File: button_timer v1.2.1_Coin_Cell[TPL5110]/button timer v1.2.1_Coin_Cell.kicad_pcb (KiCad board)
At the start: 2 copper layers, 21 x 47.8 mm, 24 parts, among them J1 Conn_01x05_Female, SW1 SW_Push, SW2 SW_Push, U1 TPS61097A, U3 TPL5111, X1 ESP-12E

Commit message: :rocket: :full_moon_with_face:
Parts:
- removed U3: TPL5111, handsolder:SOT-23-6handsoldering
- added Q1: TSM2323, Package_TO_SOT_SMD:SOT-23, F.Cu at (126.2, 64.5)
- added U2: TPL5110, handsolder:SOT-23-6handsoldering, B.Cu at (125.7, 59.0)
- C4, R8: moved to B.Cu
- C5: moved to F.Cu
- moved C4 12.6 mm to (125.4, 55.7)
- moved R7 8.05 mm to (129.6, 65.0), turned to 90 degrees
- moved SW1 7.66 mm to (128.8, 60.5), turned to 180 degrees
- moved C5 6.44 mm to (125.7, 62.0), turned to 0 degrees
- moved R8 5.66 mm to (121.7, 58.7)
- moved C3 1.86 mm to (134.8, 68.2), turned to 270 degrees
- moved L1 0.22 mm to (133.3, 60.9)
- turned D2 to 0 degrees
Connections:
- L1 pad 1: Net-(BT1-Pad1) -> Net-(L1-Pad1)
- R7 pad 2: Net-(R7-Pad2) -> Net-(L1-Pad1)
- U1 pad 1: Net-(BT1-Pad1) -> Net-(L1-Pad1)
- U1 pad 3: Net-(R7-Pad2) -> Net-(R7-Pad1)
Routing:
- net /GPIO4: track 12.2 -> 38.8 mm, vias 2 -> 1
- net Net-(BT1-Pad1): track 39.6 -> 13.5 mm, vias 9 -> 2
- net /GND: track 99.7 -> 82.7 mm, vias 18 -> 11
- net /VCC: track 55.9 -> 39.7 mm
- net Net-(Q1-Pad1): track 0.00 -> 12.3 mm, vias 0 -> 1
- net Net-(R7-Pad2): track 10.9 -> 0.00 mm, vias 1 -> 0
- net Net-(L1-Pad1): track 0.00 -> 8.00 mm, vias 0 -> 1
- net /RST: track 54.7 -> 48.7 mm, vias 4 -> 2
- net /GPIO0: track 9.39 -> 14.7 mm, vias 3 -> 0
- net Net-(R7-Pad1): track 0.00 -> 4.16 mm
- net /EN: track 18.0 -> 15.3 mm, vias 3 -> 0
- net Net-(R6-Pad2): track 16.0 -> 14.5 mm, vias 1 -> 0
- net /RX: track 7.95 -> 9.34 mm
- net Net-(D2-Pad2): track 3.24 -> 4.04 mm
- net /TX: track 14.6 -> 14.2 mm, vias 5 -> 0
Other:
- board text added: "Button - Coin Cell v.1.2.1 TPL5110"
- board text added: "V.1.2.1 ONLY COIN CELL TIMER TPL5110"
- board text removed: "Button - Coin Cell v.1.2.1"
- board text removed: "V.1.2.1 ONLY COIN CELL TIMER TPL5111"

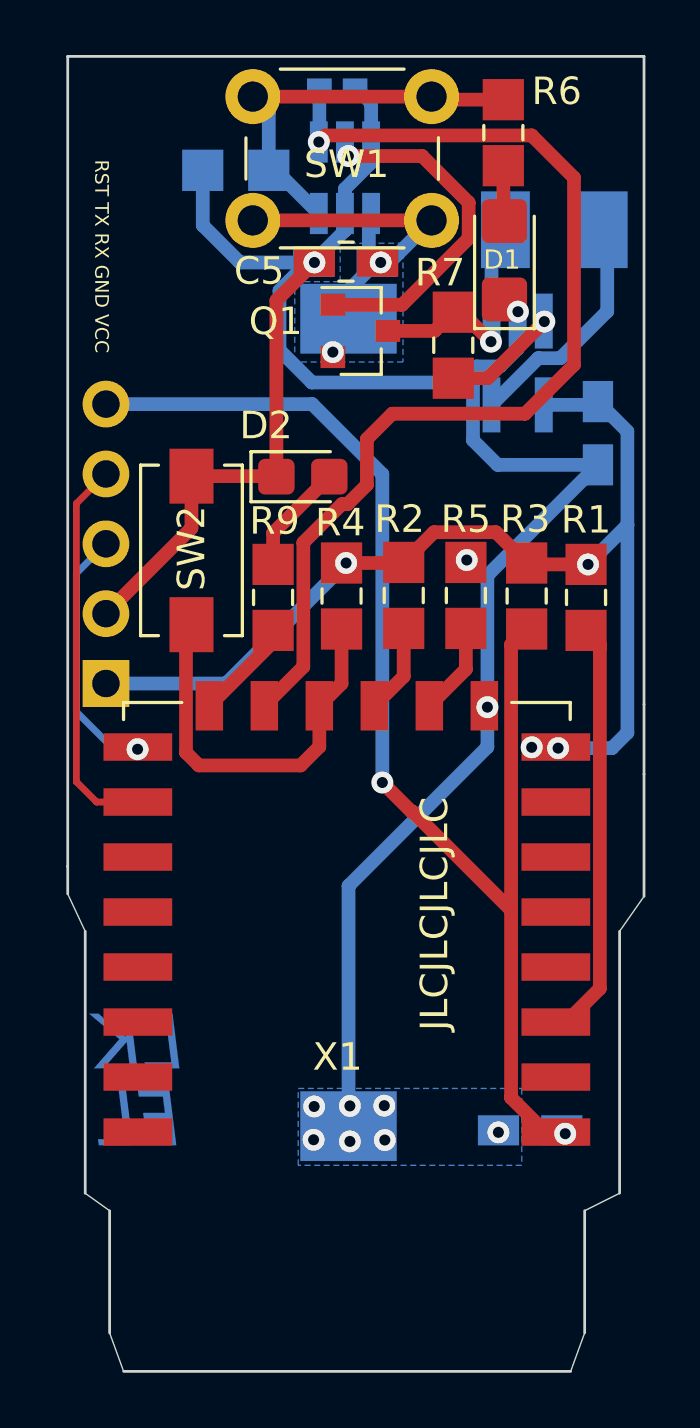
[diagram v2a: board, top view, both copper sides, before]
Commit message: 3D Models etwas verbessert
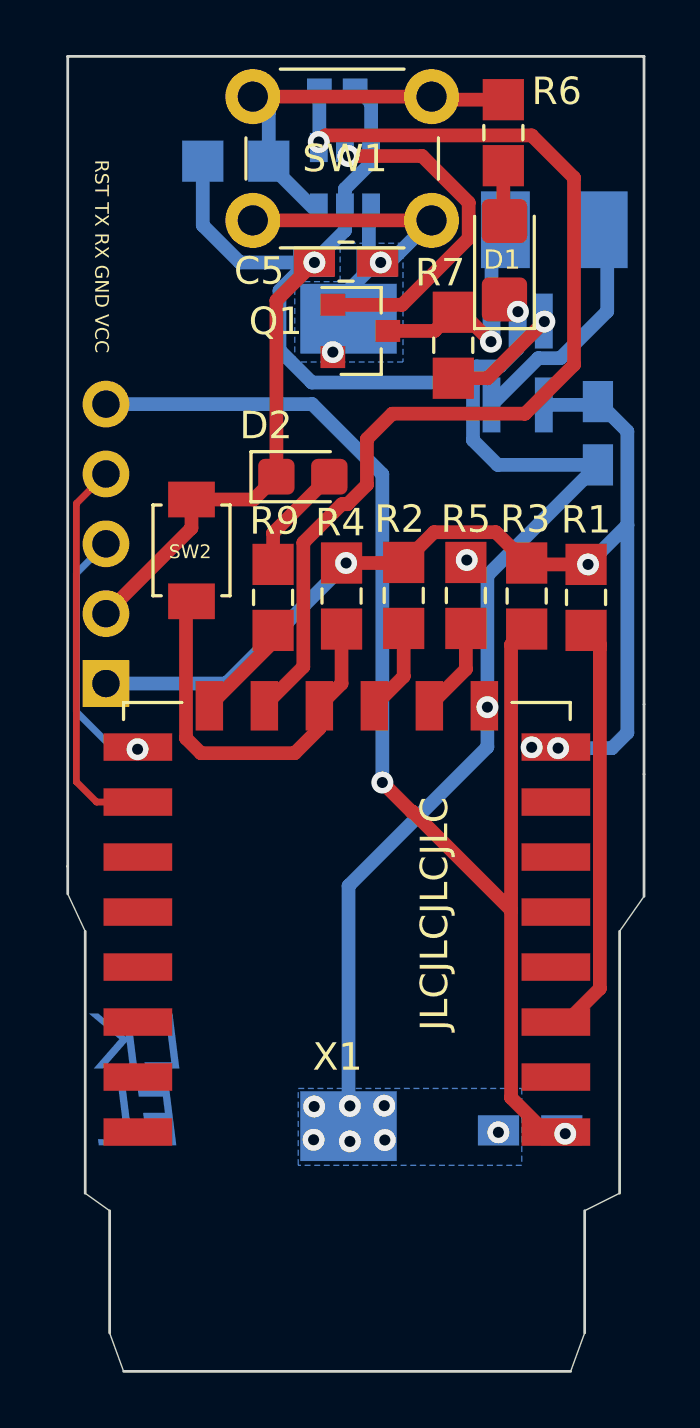
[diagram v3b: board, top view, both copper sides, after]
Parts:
- J1: footprint Connector_PinHeader_2.54mm:PinHeader_1x05_P2.54mm_Vertical -> handsolder:PinSocket_1x05_P2.54mm_Vertical_mod
- SW1: footprint Button_Switch_THT:SW_PUSH_6mm -> handsolder:SW_PUSH_6mm_H8mm_mod
- SW2: footprint Button_Switch_SMD:SW_SPST_EVQPE1 -> handsolder:SW_SPST_B3U-1000P_mod
- U2: footprint handsolder:SOT-23-6handsoldering -> Package_TO_SOT_SMD:SOT-23-6
- moved R8 0.33 mm to (121.7, 58.4)

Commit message: Silkscreen Update
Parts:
- D2: footprint LED_SMD:LED_0805_2012Metric_Castellated -> handsolder:LED_0805_2012Metric_Castellated_mod
- U2: footprint Package_TO_SOT_SMD:SOT-23-6 -> handsolder:SOT-23-6handsoldering

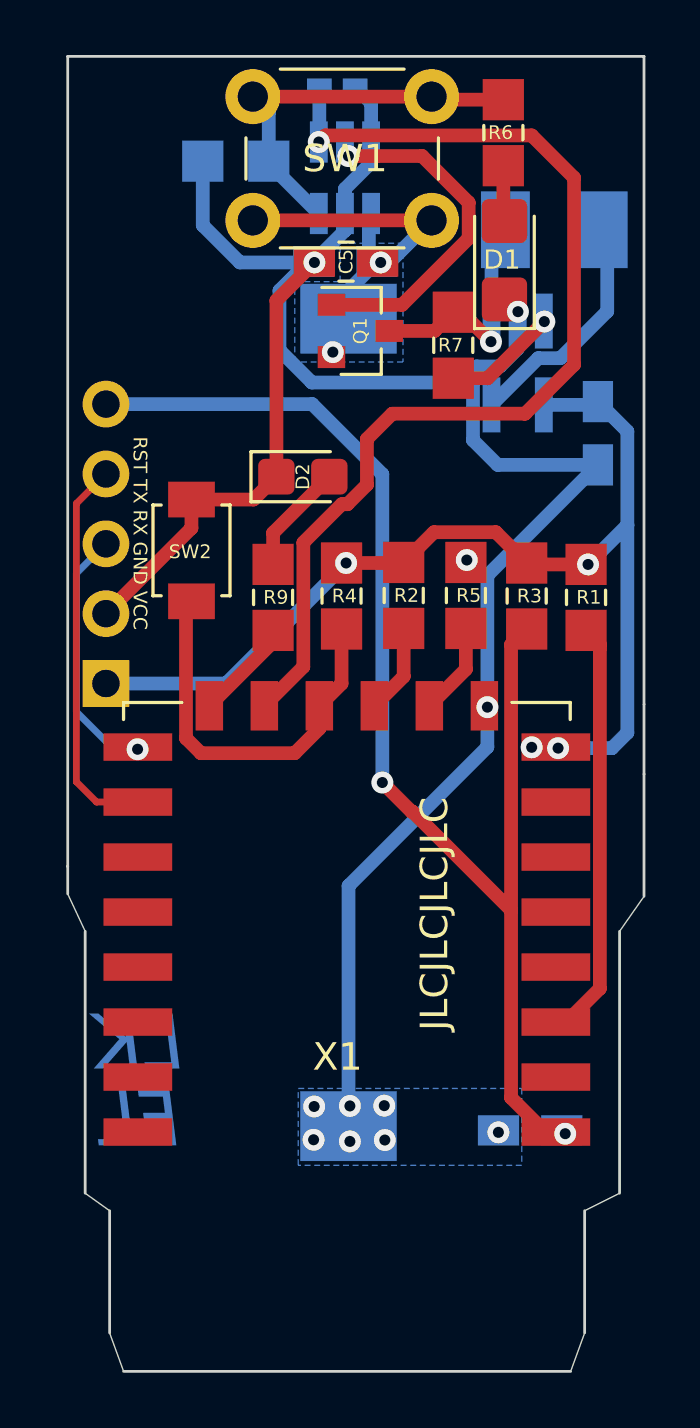
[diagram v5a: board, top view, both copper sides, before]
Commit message: cap added between vcc and gnd of the esp
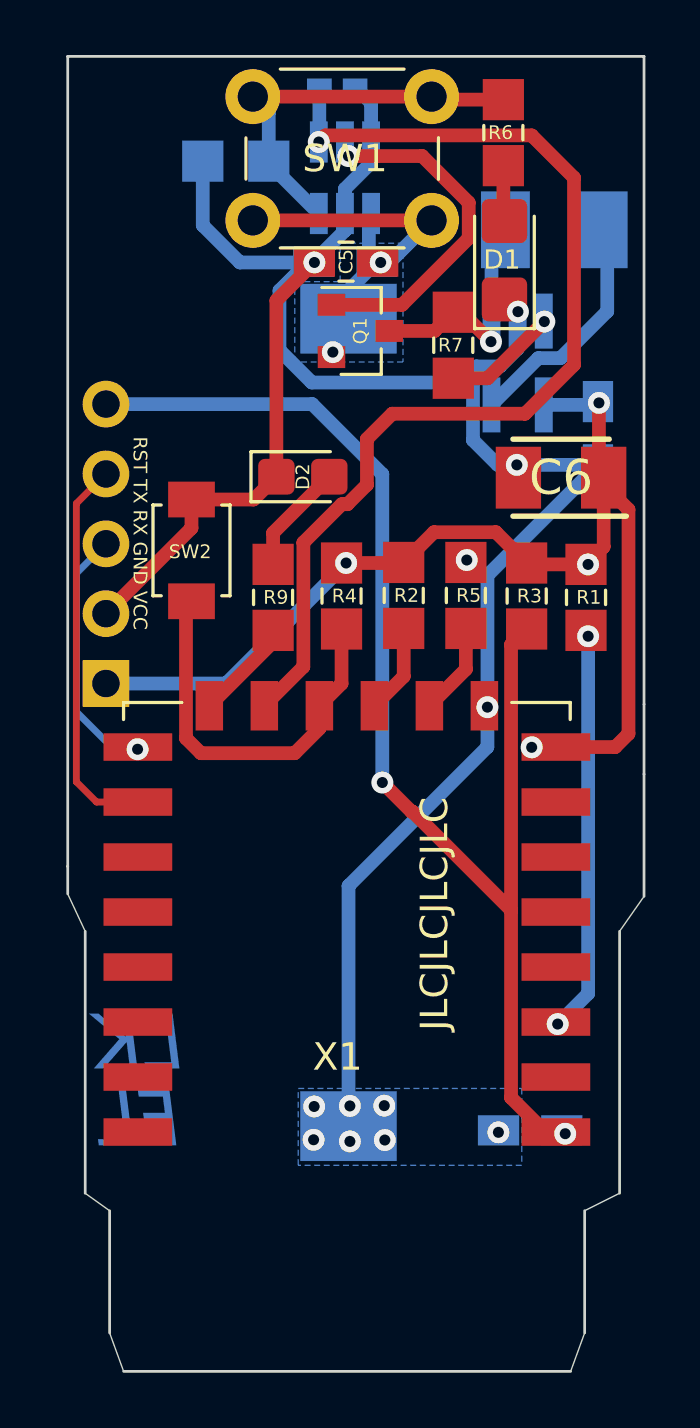
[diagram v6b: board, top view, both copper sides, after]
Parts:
- added C6: T495B476K006ATE450, SamacSys_Parts:CAPPM3528X210N, F.Cu at (133.5, 69.9)
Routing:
- net /VCC: track 39.7 -> 41.2 mm
- net /EN: track 15.3 -> 14.6 mm, vias 0 -> 2
- net /GND: vias 11 -> 12
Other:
- board text removed: "JP1 = Coin Cell JP2 = LIPO"

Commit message: Added 100nF decoupling capacitors between VCC and Ground of the ESP
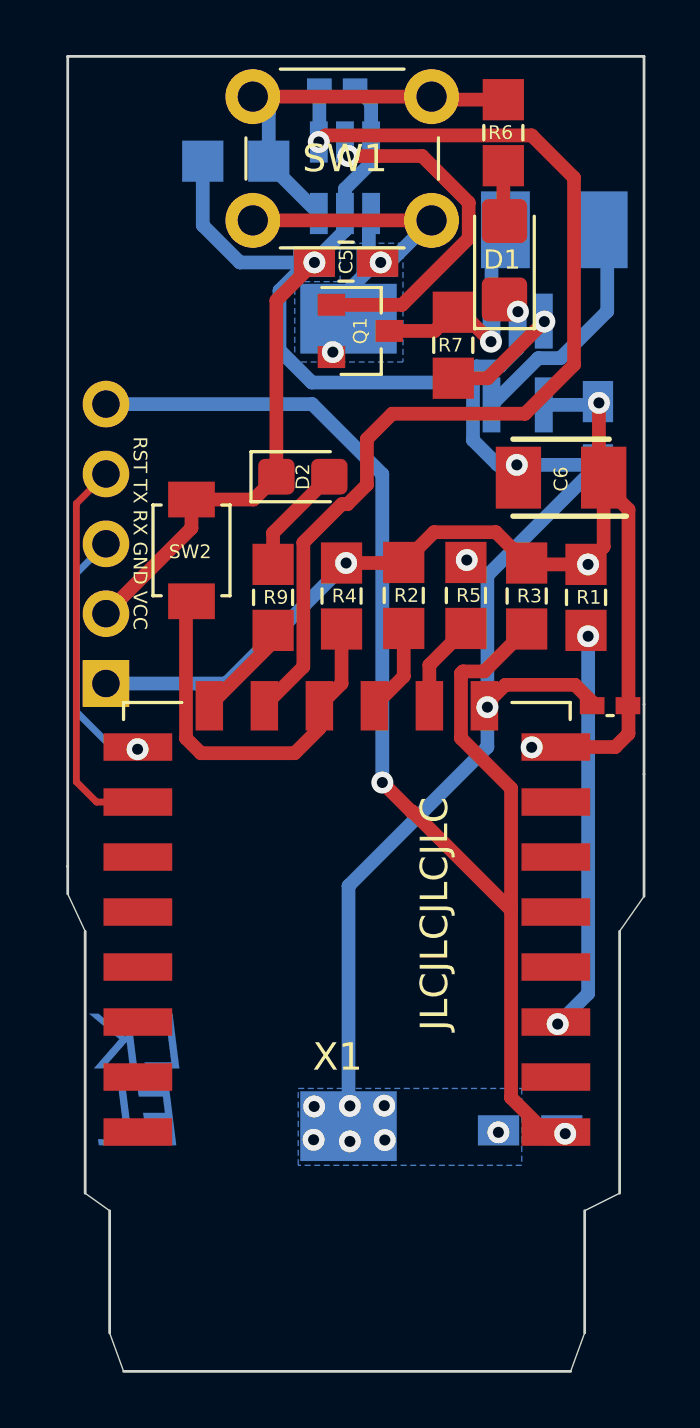
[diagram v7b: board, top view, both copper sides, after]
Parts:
- added C7: 100nF, handsolder:C_0402_1005Metric_Pad0.74x0.62mm_HandSoldermod, F.Cu at (135.3, 78.2)
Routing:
- net /GND: track 82.6 -> 87.2 mm
- net /RST: track 48.7 -> 50.7 mm
